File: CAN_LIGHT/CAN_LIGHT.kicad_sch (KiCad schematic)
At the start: 99 parts, among them IC1 MSPM0C1103SDDFR, J1 Conn_ARM_SWD_TagConnect_TC2030, J2 436500401, U1 TCAN334, U2 TPS76333DBVR, U3 NCV891330PD50R2G

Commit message: Place more LEDs and experiment with routing paths
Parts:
- renumbered C4 to C1, C11 to C10, C14 to C11, C15 to C12, C16 to C13, C17 to C14, C18 to C15, C19 to C16, C20 to C17, C21 to C18, C22 to C19, C5 to C2, C25 to C20, C28 to C21, C31 to C22, C34 to C23, C37 to C24, C23 to C25, C29 to C27, C32 to C28, C35 to C29, C6 to C3, C38 to C30, C24 to C31, C27 to C32, C30 to C33, C33 to C34, C36 to C35, C39 to C36, C40 to C37, C41 to C38, C42 to C39, C7 to C4, C43 to C40, C44 to C41, C45 to C42, C1 to C43, C2 to C44, C3 to C45, C12 to C5, C13 to C6, C8 to C7, C9 to C8, C10 to C9, D8 to D10, D22 to D20, D25 to D21, D28 to D22, D31 to D23, D34 to D24, D20 to D25, D23 to D26, D26 to D27, D29 to D28, D32 to D29, D35 to D30, D21 to D31, D24 to D32, D27 to D33, D30 to D34, D33 to D35, D9 to D5, D10 to D6, D5 to D7, D6 to D8, D7 to D9, R5 to R4, R4 to R5

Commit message: Export initial STEP file to print
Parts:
- removed J2: 436500401, 436500401:MOLEX_436500401, symbol 0436500401:436500401
- added J2: 436500428, 436500428:CON_436500428_MOL, symbol 436500428:436500428
- added J3: 430450428, 430450428:CON_430450428_MOL, symbol 430450428:430450428
- renumbered IC1 to U1, U1 to U2, U2 to U3, U3 to U4
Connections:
- net +12V: now also J2.1
- net GND: now also J2.2
- net at U2.7 (CANH): now also J2.3
- net at U2.6 (CANL): now also J2.4
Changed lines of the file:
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@@
   (symbol (lib_id "MSPM0C1103SDDFR:MSPM0C1103SDDFR") (at 62.23 236.22 0) (unit 1)
     (in_bom yes) (on_board yes) (dnp no) (fields_autoplaced)
-    (property "Reference" "IC1" (at 85.09 229.87 0)
+    (property "Reference" "U1" (at 85.09 229.87 0)
       (effects (font (size 1.27 1.27)))
     )
@@
       (project "CAN_LIGHT"
         (path "/d4f25219-6cef-4e47-aded-6c41d03d24e2"
-          (reference "IC1") (unit 1)
+          (reference "U1") (unit 1)
         )
       )
@@
     )
   )
+  (symbol (lib_id "436500428:436500428") (at 187.96 229.87 0) (unit 1)
+    (in_bom yes) (on_board yes) (dnp no) (fields_autoplaced)
+    (property "Reference" "J2" (at 201.93 232.41 0)
+      (effects (font (size 1.524 1.524)) (justify left))
+    )
+    (property "Value" "436500428" (at 201.93 234.95 0)
+      (effects (font (size 1.524 1.524)) (justify left))
+    )
+    (property "Footprint" "436500428:CON_436500428_MOL" (at 187.96 229.87 0)
+      (effects (font (size 1.27 1.27) italic) hide)
+    )
+    (property "Datasheet" "436500428" (at 187.96 229.87 0)
+      (effects (font (size 1.27 1.27) italic) hide)
+    )
+    (pin "1")
+    (pin "2")
+    (pin "3")
+    (pin "4")
+    (instances
+      (project "CAN_LIGHT"
+        (path "/d4f25219-6cef-4e47-aded-6c41d03d24e2"
+          (reference "J2") (unit 1)
+        )
+      )
+    )
+  )
   (symbol (lib_id "NCV891330PD50R2G:NCV891330PD50R2G") (at 327.66 227.33 0) (unit 1)
     (in_bom yes) (on_board yes) (dnp no) (fields_autoplaced)
-    (property "Reference" "U3" (at 347.98 217.17 0)
+    (property "Reference" "U4" (at 347.98 217.17 0)
       (effects (font (size 1.524 1.524)))
     )
@@
       (project "CAN_LIGHT"
         (path "/d4f25219-6cef-4e47-aded-6c41d03d24e2"
-          (reference "U3") (unit 1)
+          (reference "U4") (unit 1)
         )
       )
@@
     )
   )
-  (symbol (lib_id "0436500401:436500401") (at 193.04 232.41 0) (unit 1)
-    (in_bom yes) (on_board yes) (dnp no) (fields_autoplaced)
-    (property "Reference" "J2" (at 201.93 232.41 0)
-      (effects (font (size 1.27 1.27)) (justify left))
-    )
-    (property "Value" "436500401" (at 201.93 234.95 0)
-      (effects (font (size 1.27 1.27)) (justify left))
-    )
-    (property "Footprint" "436500401:MOLEX_436500401" (at 193.04 232.41 0)
-      (effects (font (size 1.27 1.27)) (justify bottom) hide)
-    )
-    (property "Datasheet" "" (at 193.04 232.41 0)
-      (effects (font (size 1.27 1.27)) hide)
-    )
-    (property "PARTREV" "D7" (at 193.04 232.41 0)
-      (effects (font (size 1.27 1.27)) (justify bottom) hide)
-    )
-    (property "STANDARD" "Manufacturer Recommendations" (at 193.04 232.41 0)
-      (effects (font (size 1.27 1.27)) (justify bottom) hide)
-    )
-    (property "MAXIMUM_PACKAGE_HEIGHT" "5.57 mm" (at 193.04 232.41 0)
-      (effects (font (size 1.27 1.27)) (justify bottom) hide)
-    )
-    (property "MANUFACTURER" "Molex" (at 193.04 232.41 0)
-      (effects (font (size 1.27 1.27)) (justify bottom) hide)
-    )
-    (pin "1")
-    (pin "2")
-    (pin "3")
-    (pin "4")
-    (instances
-      (project "CAN_LIGHT"
-        (path "/d4f25219-6cef-4e47-aded-6c41d03d24e2"
-          (reference "J2") (unit 1)
-        )
-      )
-    )
-  )
   (symbol (lib_id "power:+5V") (at 302.26 110.49 0) (mirror y) (unit 1)
     (in_bom yes) (on_board yes) (dnp no) (fields_autoplaced)
@@
   (symbol (lib_id "TPS76333DBVR:TPS76333DBVR") (at 241.3 227.33 0) (unit 1)
     (in_bom yes) (on_board yes) (dnp no) (fields_autoplaced)
-    (property "Reference" "U2" (at 250.19 213.36 0)
+    (property "Reference" "U3" (at 250.19 213.36 0)
       (effects (font (size 1.524 1.524)))
     )
@@
       (project "CAN_LIGHT"
         (path "/d4f25219-6cef-4e47-aded-6c41d03d24e2"
-          (reference "U2") (unit 1)
+          (reference "U3") (unit 1)
         )
       )
@@
     )
   )
+  (symbol (lib_id "430450428:430450428") (at 193.04 248.92 0) (unit 1)
+    (in_bom yes) (on_board yes) (dnp no) (fields_autoplaced)
+    (property "Reference" "J3" (at 207.01 251.46 0)
+      (effects (font (size 1.524 1.524)) (justify left))
+    )
+    (property "Value" "430450428" (at 207.01 254 0)
+      (effects (font (size 1.524 1.524)) (justify left))
+    )
+    (property "Footprint" "430450428:CON_430450428_MOL" (at 193.04 248.92 0)
+      (effects (font (size 1.27 1.27) italic) hide)
+    )
+    (property "Datasheet" "430450428" (at 193.04 248.92 0)
+      (effects (font (size 1.27 1.27) italic) hide)
+    )
+    (pin "1")
+    (pin "2")
+    (pin "3")
+    (pin "4")
+    (instances
+      (project "CAN_LIGHT"
+        (path "/d4f25219-6cef-4e47-aded-6c41d03d24e2"
+          (reference "J3") (unit 1)
+        )
+      )
+    )
+  )
   (symbol (lib_id "Device:C") (at 153.67 149.86 0) (unit 1)
     (in_bom yes) (on_board yes) (dnp no)
@@
   (symbol (lib_id "Interface_CAN_LIN:TCAN334") (at 161.29 237.49 0) (unit 1)
     (in_bom yes) (on_board yes) (dnp no) (fields_autoplaced)
-    (property "Reference" "U1" (at 163.4841 224.79 0)
+    (property "Reference" "U2" (at 163.4841 224.79 0)
       (effects (font (size 1.27 1.27)) (justify left))
     )
@@
       (project "CAN_LIGHT"
         (path "/d4f25219-6cef-4e47-aded-6c41d03d24e2"
-          (reference "U1") (unit 1)
+          (reference "U2") (unit 1)
         )
       )

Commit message: Select new MCU with CAN controller peripheral included
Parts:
- added C46, C47, C48, C49, C50, C51, C52, C53, C54, C55, C56, C57, C58, C59, C60, C61, C62, C63, C64, C65, C66, C67, C68, C69, C70, C71, C72, C73, C74, C75, C76, C77, C78, C79, C80, C81, C82, C83, C84, C85, C86, C87: 0.1uF, Capacitor_SMD:C_0603_1608Metric_Pad1.08x0.95mm_HandSolder, symbol Device:C
- added D43, D44, D45, D46, D47, D48, D49, D50, D51, D52, D53, D54, D55, D56, D57, D58, D59, D60, D61, D62, D63, D64, D65, D66, D67, D68, D69, D70, D71, D72, D73, D74, D75, D76, D77, D78, D79, D80, D81, D82, D83, D84: ~, IN-PI4818QAS5R5G5BPW:INPI4818QAS5R5G5BPW, symbol LED:IN-PI4818QAS5R5G5BPW
- added J4: Conn_ARM_SWD_TagConnect_TC2030-NL, Connector:Tag-Connect_TC2030-IDC-NL_2x03_P1.27mm_Vertical, symbol Connector:Conn_ARM_SWD_TagConnect_TC2030-NL
- added U5: XMSM0G3507SDGS28R, VSSOP28_DGS_TEX, symbol MSPM0G3507SDGS28R:XMSM0G3507SDGS28R
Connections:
- net +5V: now also C46.1, C47.1, C48.1, C49.1, C50.1, C51.1, C52.1, C53.1, C54.1, C55.1, C56.1, C57.1, C58.1, C59.1, C60.1, C61.1, C62.1, C63.1, C64.1, C65.1, C66.1, C67.1, C68.1, C69.1, C70.1, C71.1, C72.1, C73.1, C74.1, C75.1, C76.1, C77.1, C78.1, C79.1, C80.1, C81.1, C82.1, C83.1, C84.1, C85.1, C86.1, C87.1, D43.1 (W-VDD), D43.5 (VDD), D44.1 (W-VDD), D44.5 (VDD), D45.1 (W-VDD), D45.5 (VDD), D46.1 (W-VDD), D46.5 (VDD), D47.1 (W-VDD), D47.5 (VDD), D48.1 (W-VDD), D48.5 (VDD), D49.1 (W-VDD), D49.5 (VDD), D50.1 (W-VDD), D50.5 (VDD), D51.1 (W-VDD), D51.5 (VDD), D52.1 (W-VDD), D52.5 (VDD), D53.1 (W-VDD), D53.5 (VDD), D54.1 (W-VDD), D54.5 (VDD), D55.1 (W-VDD), D55.5 (VDD), D56.1 (W-VDD), D56.5 (VDD), D57.1 (W-VDD), D57.5 (VDD), D58.1 (W-VDD), D58.5 (VDD), D59.1 (W-VDD), D59.5 (VDD), D60.1 (W-VDD), D60.5 (VDD), D61.1 (W-VDD), D61.5 (VDD), D62.1 (W-VDD), D62.5 (VDD), D63.1 (W-VDD), D63.5 (VDD), D64.1 (W-VDD), D64.5 (VDD), D65.1 (W-VDD), D65.5 (VDD), D66.1 (W-VDD), D66.5 (VDD), D67.1 (W-VDD), D67.5 (VDD), D68.1 (W-VDD), D68.5 (VDD), D69.1 (W-VDD), D69.5 (VDD), D70.1 (W-VDD), D70.5 (VDD), D71.1 (W-VDD), D71.5 (VDD), D72.1 (W-VDD), D72.5 (VDD), D73.1 (W-VDD), D73.5 (VDD), D74.1 (W-VDD), D74.5 (VDD), D75.1 (W-VDD), D75.5 (VDD), D76.1 (W-VDD), D76.5 (VDD), D77.1 (W-VDD), D77.5 (VDD), D78.1 (W-VDD), D78.5 (VDD), D79.1 (W-VDD), D79.5 (VDD), D80.1 (W-VDD), D80.5 (VDD), D81.1 (W-VDD), D81.5 (VDD), D82.1 (W-VDD), D82.5 (VDD), D83.1 (W-VDD), D83.5 (VDD), D84.1 (W-VDD), D84.5 (VDD)
- net GND: now also C46.2, C47.2, C48.2, C49.2, C50.2, C51.2, C52.2, C53.2, C54.2, C55.2, C56.2, C57.2, C58.2, C59.2, C60.2, C61.2, C62.2, C63.2, C64.2, C65.2, C66.2, C67.2, C68.2, C69.2, C70.2, C71.2, C72.2, C73.2, C74.2, C75.2, C76.2, C77.2, C78.2, C79.2, C80.2, C81.2, C82.2, C83.2, C84.2, C85.2, C86.2, C87.2, D43.4 (GND), D44.4 (GND), D45.4 (GND), D46.4 (GND), D47.4 (GND), D48.4 (GND), D49.4 (GND), D50.4 (GND), D51.4 (GND), D52.4 (GND), D53.4 (GND), D54.4 (GND), D55.4 (GND), D56.4 (GND), D57.4 (GND), D58.4 (GND), D59.4 (GND), D60.4 (GND), D61.4 (GND), D62.4 (GND), D63.4 (GND), D64.4 (GND), D65.4 (GND), D66.4 (GND), D67.4 (GND), D68.4 (GND), D69.4 (GND), D70.4 (GND), D71.4 (GND), D72.4 (GND), D73.4 (GND), D74.4 (GND), D75.4 (GND), D76.4 (GND), D77.4 (GND), D78.4 (GND), D79.4 (GND), D80.4 (GND), D81.4 (GND), D82.4 (GND), D83.4 (GND), D84.4 (GND)
- net at D42.3 (DOUT): now also D43.6 (DIN)
- new net: D81.3 (DOUT), D82.6 (DIN)
- new net: D80.3 (DOUT), D81.6 (DIN)
- new net: D69.3 (DOUT), D70.6 (DIN)
- new net: D68.3 (DOUT), D69.6 (DIN)
- new net: D67.3 (DOUT), D68.6 (DIN)
- new net: D61.3 (DOUT), D62.6 (DIN)
- new net: D60.3 (DOUT), D61.6 (DIN)
- new net: D71.3 (DOUT), D72.6 (DIN)
- new net: D70.3 (DOUT), D71.6 (DIN)
- new net: D47.3 (DOUT), D48.6 (DIN)
- new net: D46.3 (DOUT), D47.6 (DIN)
- new net: D74.3 (DOUT), D75.6 (DIN)
- new net: D73.3 (DOUT), D74.6 (DIN)
- new net: D59.3 (DOUT), D60.6 (DIN)
- new net: D54.3 (DOUT), D55.6 (DIN)
- new net: D53.3 (DOUT), D54.6 (DIN)
- new net: D43.3 (DOUT), D44.6 (DIN)
- new net: D77.3 (DOUT), D78.6 (DIN)
- new net: D76.3 (DOUT), D77.6 (DIN)
- new net: D83.3 (DOUT), D84.6 (DIN)
- new net: D82.3 (DOUT), D83.6 (DIN)
- new net: D65.3 (DOUT), D66.6 (DIN)
- new net: D64.3 (DOUT), D65.6 (DIN)
- new net: D72.3 (DOUT), D73.6 (DIN)
- new net: J4.2 (SWDIO), U5.22 (PA19/SWDIO)
- new net: J4.4 (SWCLK), U5.23 (PA20/SWCLK)
- new net: J4.3 (~{RESET}), U5.6 (NRST)
- new net: D44.3 (DOUT), D45.6 (DIN)
- new net: D62.3 (DOUT), D63.6 (DIN)
- new net: D63.3 (DOUT), D64.6 (DIN)
- new net: D75.3 (DOUT), D76.6 (DIN)
- new net: D56.3 (DOUT), D57.6 (DIN)
- new net: D55.3 (DOUT), D56.6 (DIN)
- new net: D48.3 (DOUT), D49.6 (DIN)
- new net: D78.3 (DOUT), D79.6 (DIN)
- new net: D49.3 (DOUT), D50.6 (DIN)
- new net: D58.3 (DOUT), D59.6 (DIN)
- new net: D57.3 (DOUT), D58.6 (DIN)
- new net: D79.3 (DOUT), D80.6 (DIN)
- new net: D52.3 (DOUT), D53.6 (DIN)
- new net: D51.3 (DOUT), D52.6 (DIN)
- new net: D45.3 (DOUT), D46.6 (DIN)
- new net: D66.3 (DOUT), D67.6 (DIN)
- new net: D50.3 (DOUT), D51.6 (DIN)
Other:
- moved on the sheet: C1, C10, C11, C12, C13, C14, C15, C16, C17, C18, C19, C2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

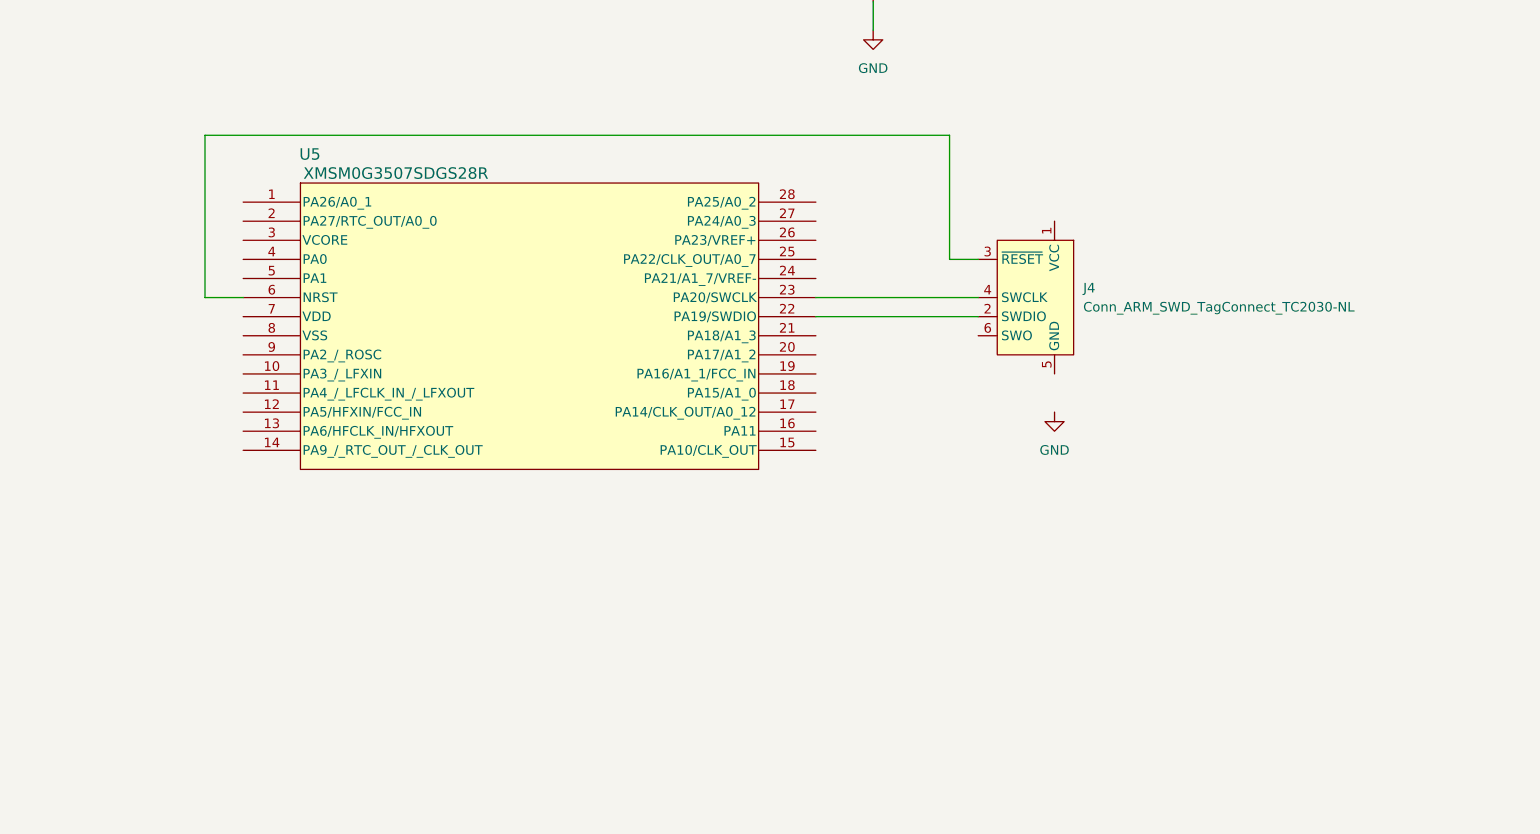
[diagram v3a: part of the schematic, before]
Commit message: Add passives to MCU
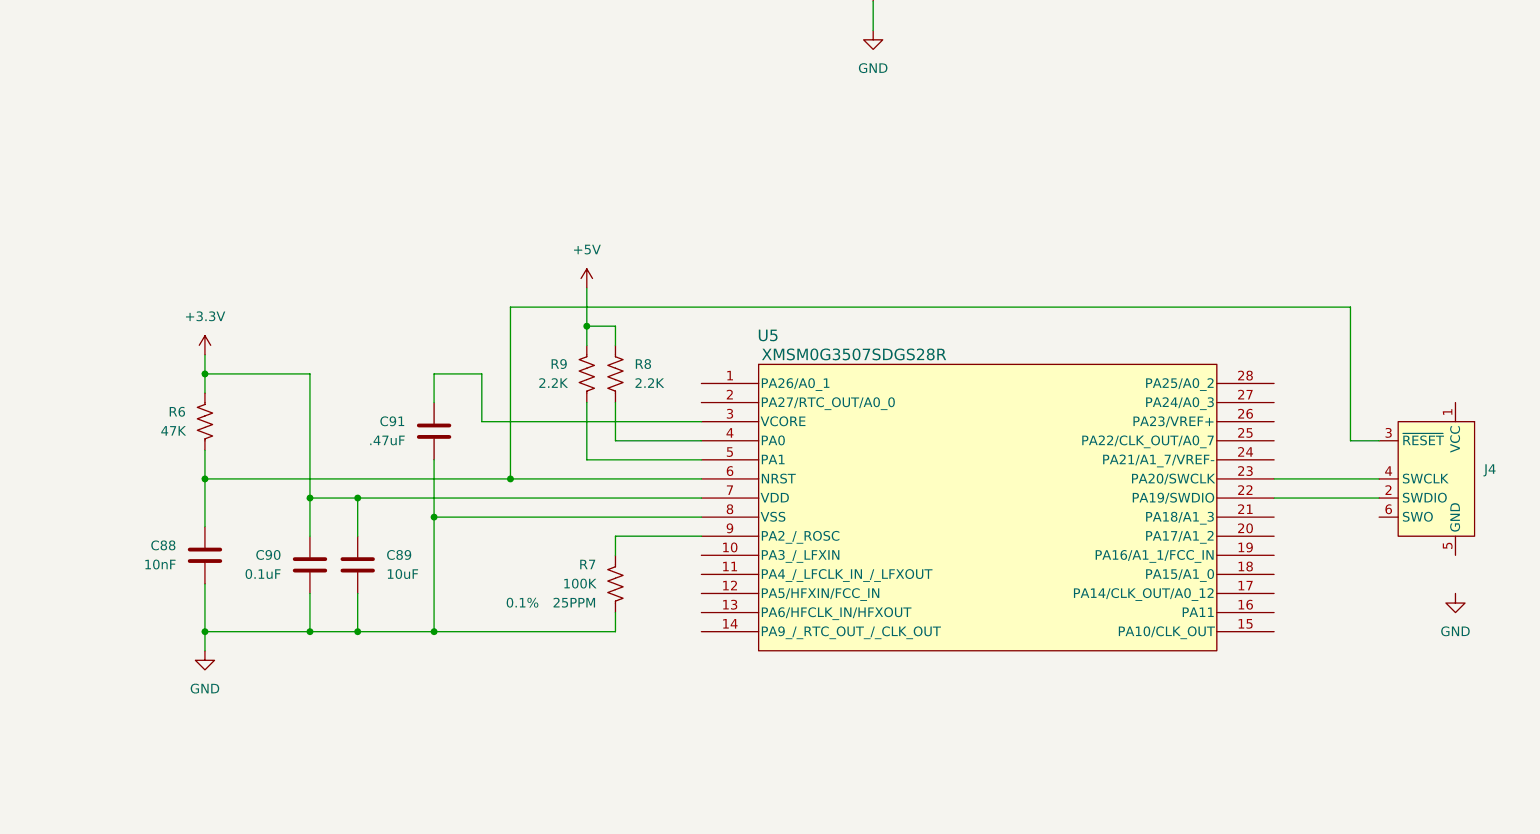
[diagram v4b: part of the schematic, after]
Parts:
- added C88: 10nF, Capacitor_SMD:C_0603_1608Metric_Pad1.08x0.95mm_HandSolder, symbol Device:C
- added C89: 10uF, Capacitor_SMD:C_0603_1608Metric_Pad1.08x0.95mm_HandSolder, symbol Device:C
- added C90: 0.1uF, Capacitor_SMD:C_0603_1608Metric_Pad1.08x0.95mm_HandSolder, symbol Device:C
- added C91: .47uF, Capacitor_SMD:C_0603_1608Metric_Pad1.08x0.95mm_HandSolder, symbol Device:C
- added R6: 47K, Resistor_SMD:R_0603_1608Metric_Pad0.98x0.95mm_HandSolder, symbol Device:R_US
- added R7: 100K, Resistor_SMD:R_0603_1608Metric_Pad0.98x0.95mm_HandSolder, symbol Device:R_US
- added R8, R9: 2.2K, Resistor_SMD:R_0603_1608Metric_Pad0.98x0.95mm_HandSolder, symbol Device:R_US
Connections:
- net +3.3V: now also U5.7 (VDD), C89.1, C90.1, R6.1
- net +5V: now also R8.1, R9.1
- net GND: now also U5.8 (VSS), C88.2, C89.2, C90.2, C91.2, R7.2
- net at U5.3 (VCORE): now also C91.1
- net at U5.4 (PA0): now also R8.2
- net at U5.5 (PA1): now also R9.2
- net at J4.3 (~{RESET}), U5.6 (NRST): now also C88.1, R6.2
- net at U5.9 (PA2_/_ROSC): now also R7.1
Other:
- moved on the sheet: J4, U5

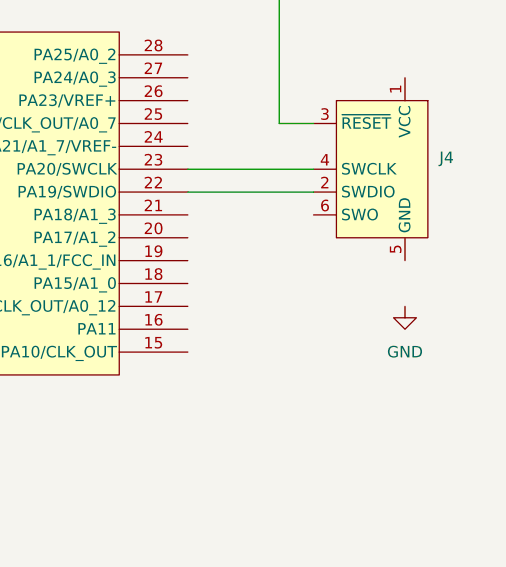
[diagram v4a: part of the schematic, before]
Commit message: Update LED routing
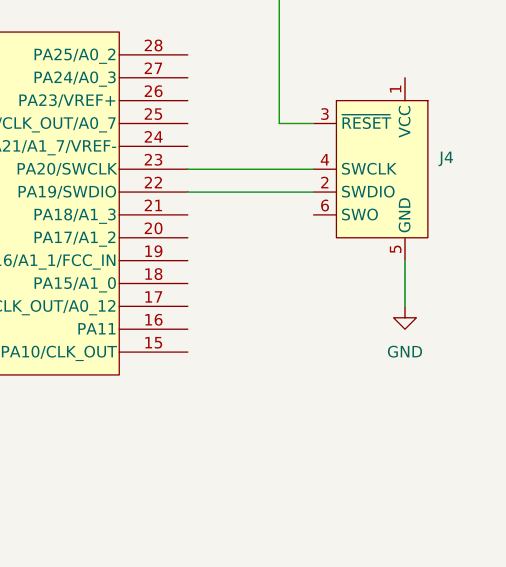
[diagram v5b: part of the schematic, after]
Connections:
- net GND: now also J4.5 (GND)
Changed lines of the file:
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@@
+    (stroke (width 0) (type default))
+  )
+  (wire (pts (xy 571.5 154.94) (xy 571.5 160.02))
     (stroke (width 0) (type default))
   )
